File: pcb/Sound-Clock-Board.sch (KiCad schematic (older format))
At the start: 5 parts, among them J1 ESPThingLeftSide, J2 ESPThingRightSide, J3 I2SBoard, J4 ToConfigBtn, J5 ToTouchPlate

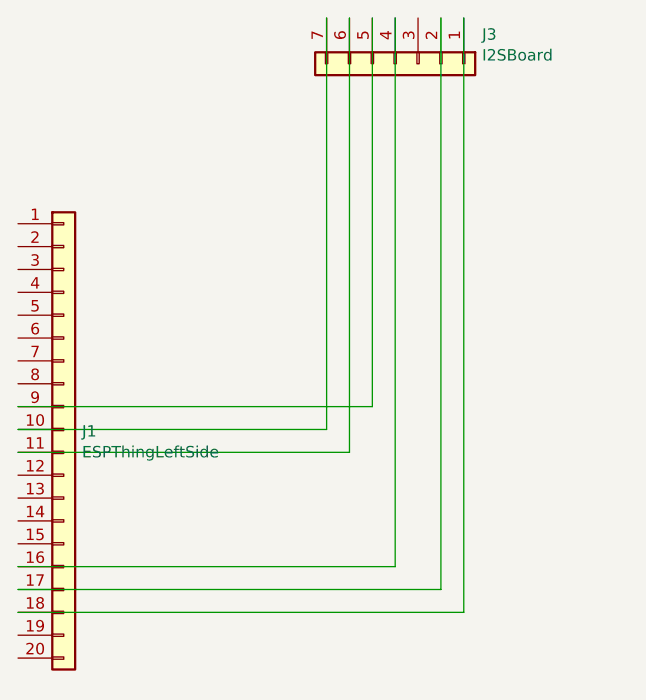
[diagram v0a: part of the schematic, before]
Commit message: Fixed an incorrect trace
I had a trace going to the VBAT pin that should have been going to VUSB.  Worked when not plugged in, or when in a breadboard, but didn't work on the circuit boards I milled.
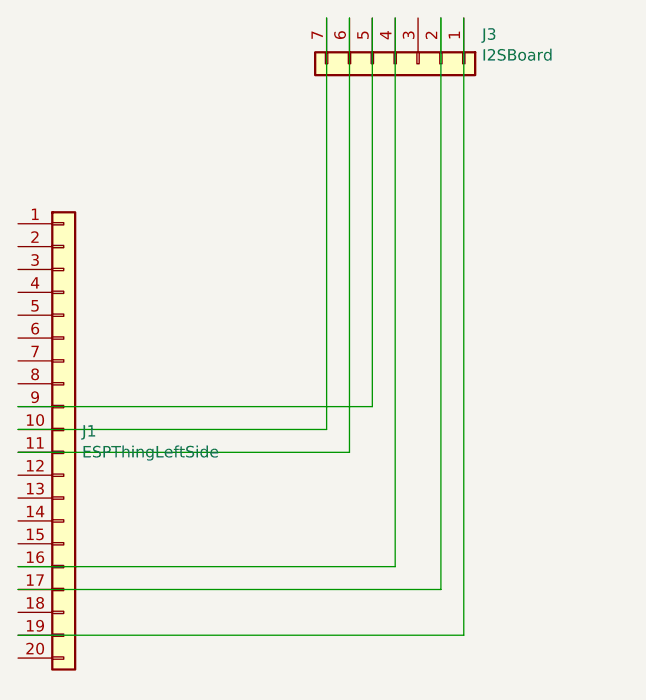
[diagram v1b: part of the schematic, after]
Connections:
- net at J1.18 (Pin_18): no longer J3.1 (Pin_1)
- net at J1.19 (Pin_19): now also J3.1 (Pin_1)
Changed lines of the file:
@@
 $EndComp
-Wire Wire Line
-	3000 5350 4950 5350
-Wire Wire Line
-	4950 5350 4950 2750
 Wire Wire Line
 	3000 5250 4850 5250
@@
 Wire Wire Line
 	7350 3600 7700 3600
+Wire Wire Line
+	4950 5450 3000 5450
+Wire Wire Line
+	4950 2750 4950 5450
 $EndSCHEMATC

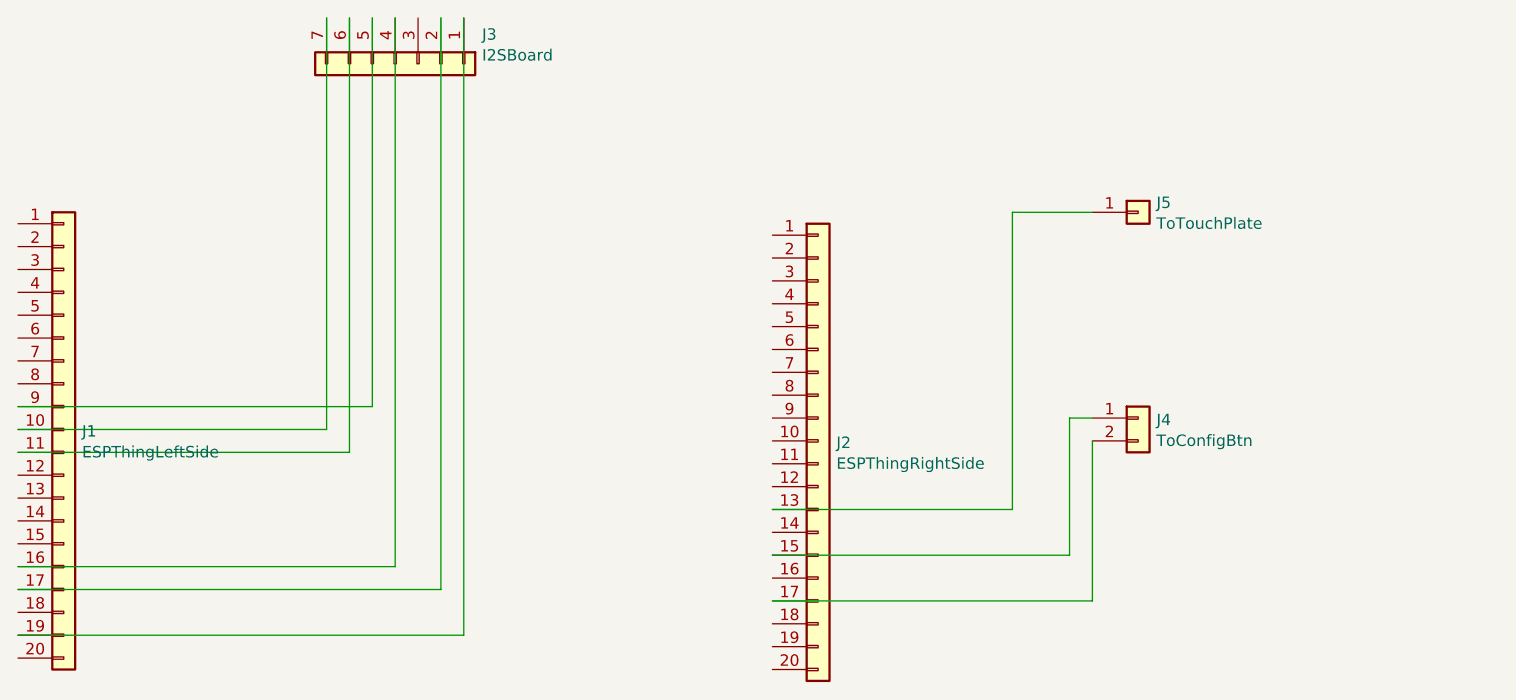
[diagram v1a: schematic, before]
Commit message: Added gain control and merged the single pin header with the two pin header for strength
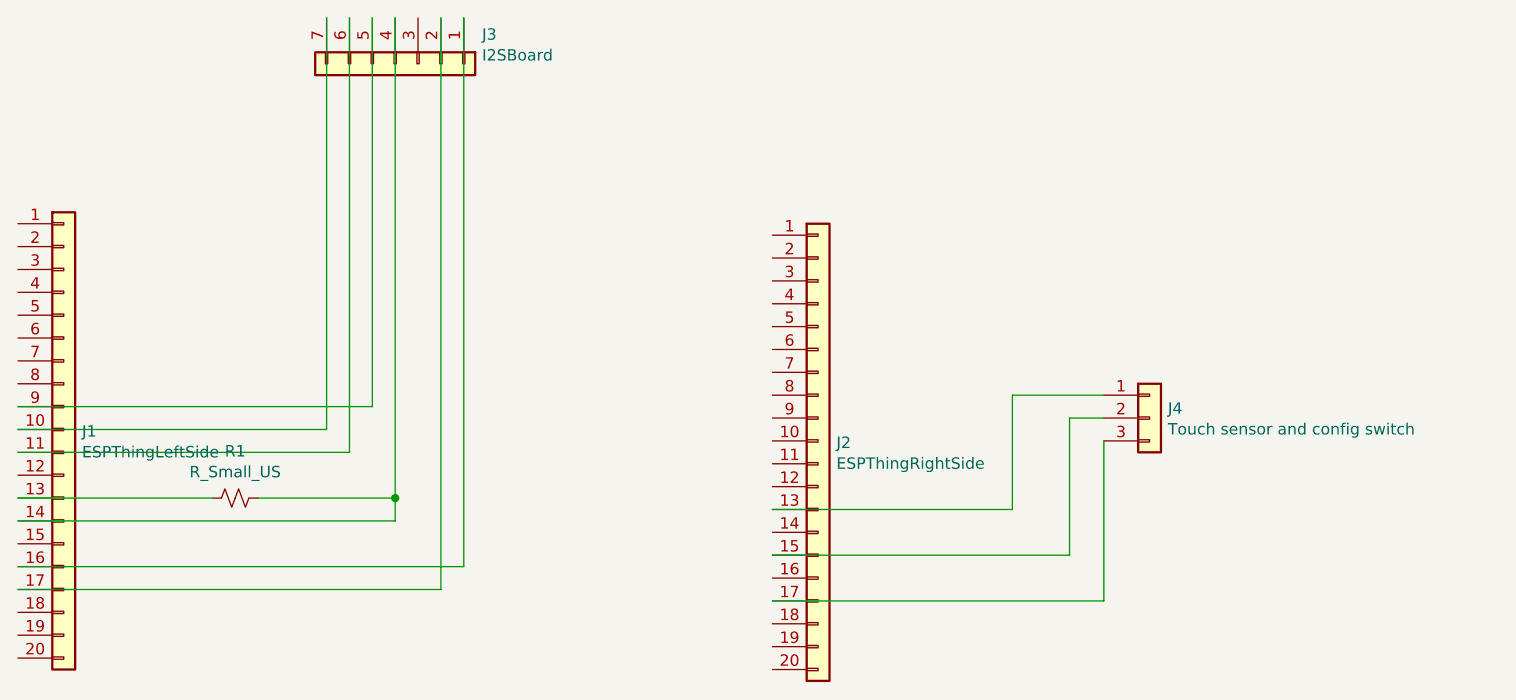
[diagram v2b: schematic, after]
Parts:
- removed J4: ToConfigBtn, Connector_PinHeader_2.54mm:PinHeader_1x02_P2.54mm_Vertical, symbol Connector_Generic:Conn_01x02
- removed J5: ToTouchPlate, Connector_PinHeader_2.54mm:PinHeader_1x01_P2.54mm_Vertical, symbol Connector_Generic:Conn_01x01
- added J4: Touch sensor and config switch, Connector_PinHeader_2.54mm:PinHeader_1x03_P2.54mm_Vertical, symbol Connector_Generic:Conn_01x03
- added R1: R_Small_US, Resistor_THT:R_Axial_DIN0207_L6.3mm_D2.5mm_P2.54mm_Vertical, symbol Device:R_Small_US
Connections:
- net at J1.13 (Pin_13): now also R1.2
- net at J1.14 (Pin_14): now also J3.4 (Pin_4), R1.1
- net at J1.16 (Pin_16): now also J3.1 (Pin_1); no longer J3.4 (Pin_4)
- net at J1.19 (Pin_19): no longer J3.1 (Pin_1)
- net at J2.13 (Pin_13): now also J4.1 (Pin_1)
- net at J2.15 (Pin_15): now also J4.2 (Pin_2)
- net at J2.17 (Pin_17): now also J4.3 (Pin_3)
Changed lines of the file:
@@
-$EndComp
-$Comp
-L Connector_Generic:Conn_01x01 J5
-U 1 1 5FC0C89E
-P 7900 3600
-F 0 "J5" H 7980 3642 50  0000 L CNN
-F 1 "ToTouchPlate" H 7980 3551 50  0000 L CNN
-F 2 "Connector_PinHeader_2.54mm:PinHeader_1x01_P2.54mm_Vertical" H 7900 3600 50  0001 C CNN
-F 3 "~" H 7900 3600 50  0001 C CNN
-	1    7900 3600
-	1    0    0    -1
-$EndComp
-$Comp
-L Connector_Generic:Conn_01x02 J4
-U 1 1 5FC0CC94
-P 7900 4500
-F 0 "J4" H 7980 4492 50  0000 L CNN
-F 1 "ToConfigBtn" H 7980 4401 50  0000 L CNN
-F 2 "Connector_PinHeader_2.54mm:PinHeader_1x02_P2.54mm_Vertical" H 7900 4500 50  0001 C CNN
-F 3 "~" H 7900 4500 50  0001 C CNN
-	1    7900 4500
-	1    0    0    -1
 $EndComp
 $Comp
@@
 	4850 5250 4850 2750
 Wire Wire Line
-	3000 5150 4650 5150
-Wire Wire Line
-	4650 5150 4650 2750
-Wire Wire Line
 	3000 4650 4450 4650
 Wire Wire Line
@@
 	4550 4450 4550 2750
 Wire Wire Line
-	6300 5300 7700 5300
+	6300 5300 7750 5300
 Wire Wire Line
-	7700 5300 7700 4600
+	7750 5300 7750 4600
 Wire Wire Line
 	6300 5100 7600 5100
@@
 	7600 5100 7600 4500
 Wire Wire Line
-	7600 4500 7700 4500
+	7600 4500 7750 4500
 Wire Wire Line
 	6300 4900 7350 4900
 Wire Wire Line
-	7350 4900 7350 3600
+	7350 4900 7350 4400
 Wire Wire Line
-	7350 3600 7700 3600
+	7350 4400 7750 4400
+$Comp
+L Connector_Generic:Conn_01x03 J4
+U 1 1 5FC97F1D
+P 7950 4500
+F 0 "J4" H 8030 4542 50  0000 L CNN
+F 1 "Touch sensor and config switch" H 8030 4451 50  0000 L CNN
+F 2 "Connector_PinHeader_2.54mm:PinHeader_1x03_P2.54mm_Vertical" H 7950 4500 50  0001 C CNN
+F 3 "~" H 7950 4500 50  0001 C CNN
+	1    7950 4500
+	1    0    0    -1
+$EndComp
 Wire Wire Line
-	4950 5450 3000 5450
+	4950 5150 4950 2750
 Wire Wire Line
-	4950 2750 4950 5450
+	3000 5150 4950 5150
+Wire Wire Line
+	3000 4850 3850 4850
+Wire Wire Line
+	3000 4950 4650 4950
+Wire Wire Line
+	4650 4950 4650 4850
+$Comp
+L Device:R_Small_US R1
+U 1 1 5FCA8101
+P 3950 4850
+F 0 "R1" V 3745 4850 50  0000 C CNN
+F 1 "R_Small_US" V 3836 4850 50  0000 C CNN
+F 2 "Resistor_THT:R_Axial_DIN0207_L6.3mm_D2.5mm_P2.54mm_Vertical" H 3950 4850 50  0001 C CNN
+F 3 "~" H 3950 4850 50  0001 C CNN
+	1    3950 4850
+	0    1    1    0
+$EndComp
+Wire Wire Line
+	4050 4850 4650 4850
+Connection ~ 4650 4850
+Wire Wire Line
+	4650 4850 4650 2750
 $EndSCHEMATC
